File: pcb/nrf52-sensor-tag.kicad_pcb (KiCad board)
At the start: 2 copper layers, 36 x 33 mm, 23 parts, among them IC1 LTR-308ALS-01, IC3 MS860702BA01-50, J3 Conn_01x07_Male, SW1 EVQ-PUA02K, SW2 EVQ-PUA02K, U1 MS88SF2

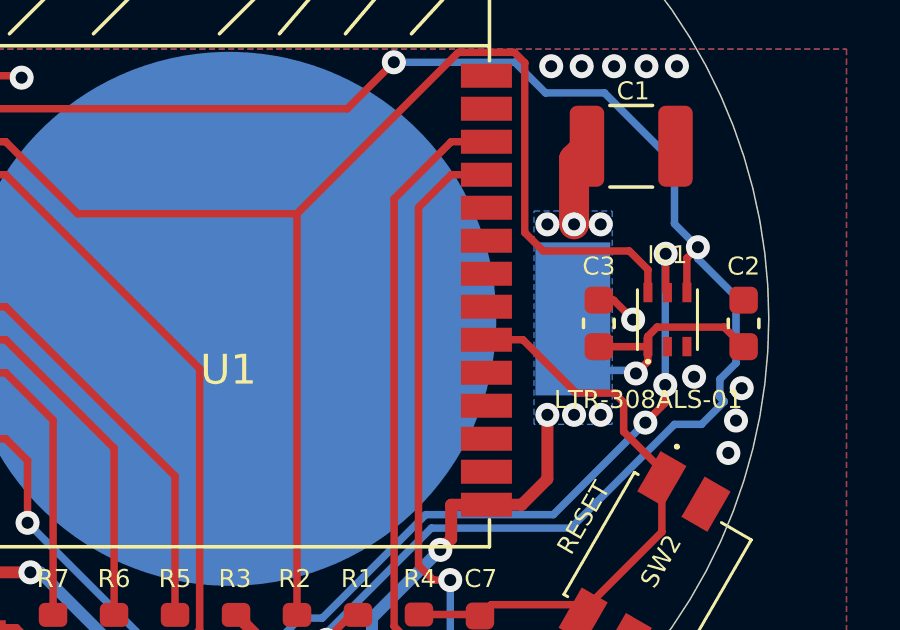
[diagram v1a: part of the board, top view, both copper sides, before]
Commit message: Fixed DRC issues
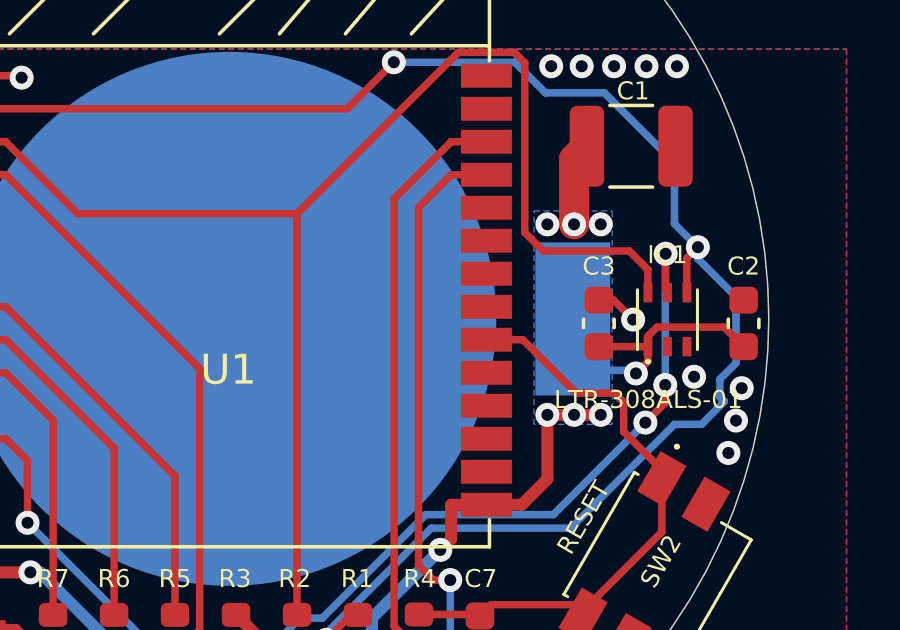
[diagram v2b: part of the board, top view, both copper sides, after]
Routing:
- net /VCC: track 74.2 -> 75.9 mm
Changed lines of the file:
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@@
     (property "Sheetname" "")
     (attr smd)
-    (fp_text reference "BT1" (at 0 0) (layer "B.SilkS")
+    (fp_text reference "BT1" (at 0 0) (layer "B.SilkS") hide
       (effects (font (size 1.27 1.27) (thickness 0.254)) (justify mirror))
     )
@@
   (segment (start 106.0257 61.9699) (end 109.2806 58.715) (width 0.25) (layer "F.Cu") (net 3))
   (segment (start 131.2708 55.7348) (end 131.6184 56.0824) (width 0.25) (layer "F.Cu") (net 3))
-  (segment (start 124.0529 61.0863) (end 124.026 61.1132) (width 0.25) (layer "F.Cu") (net 3))
   (segment (start 109.2806 58.715) (end 113.14 58.715) (width 0.25) (layer "F.Cu") (net 3))
   (segment (start 113.14 58.715) (end 114.3153 58.715) (width 0.25) (layer "F.Cu") (net 3))
@@
   (segment (start 111.9647 72.1121) (end 112.9207 73.0681) (width 0.4) (layer "F.Cu") (net 11))
   (segment (start 124.435 79.3623) (end 124.435 78.187) (width 0.4) (layer "F.Cu") (net 11))
+  (segment (start 132.372 67.818) (end 134.15 67.818) (width 0.4) (layer "F.Cu") (net 11))
   (segment (start 107.8087 68.395) (end 106.9644 67.5507) (width 0.4) (layer "F.Cu") (net 11))
   (segment (start 135.723 65.199489) (end 135.723 65.543) (width 0.25) (layer "F.Cu") (net 11))
